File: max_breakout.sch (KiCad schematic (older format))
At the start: 29 parts, among them J1 AVR-JTAG-10, J2 Conn_01x16, J3 Conn_01x16, J4 USB_B_Micro, SW1 SW_DIP_x06, U1 CPLD - EPM7032STC44, X1 KC5032K12.0000C10E00-Oscillat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

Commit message: switched to 32pins
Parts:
- U1: symbol sbc_z80-rescue:EPM7032STC44-CPLD_Altera -> max_breakout-rescue:EPM7032STC44-CPLD_Altera-sbc_z80-rescue
- X1: symbol rc2014_max_v-rescue:KC5032K12.0000C10E00-Oscillator -> max_breakout-rescue:KC5032K12.0000C10E00-Oscillator-rc2014_max_v-rescue
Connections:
- wire segments 174 -> 180
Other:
- moved on the sheet: R15
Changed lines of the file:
@@
 EESchema Schematic File Version 4
-LIBS:sbc_z80-cache
+LIBS:max_breakout-cache
 EELAYER 29 0
 EELAYER END
@@
 $EndDescr
 $Comp
-L sbc_z80-rescue:EPM7032STC44-CPLD_Altera U1
+L max_breakout-rescue:EPM7032STC44-CPLD_Altera-sbc_z80-rescue U1
 U 1 1 5D1470E3
 P 4595 2740
@@
 L Device:C_Small C?
 U 1 1 5D617C96
-P 1005 1585
+P 1046 1798
 AR Path="/5D65A6A0/5D617C96" Ref="C?"  Part="1"
 AR Path="/5D617C96" Ref="C1"  Part="1"
-F 0 "C1" H 1097 1631 50  0000 L CNN
-F 1 "100nF" H 1097 1540 50  0000 L CNN
-F 2 "Capacitor_SMD:C_0603_1608Metric_Pad1.05x0.95mm_HandSolder" H 1005 1585 50  0001 C CNN
-F 3 "https://www.mouser.com/datasheet/2/396/mlcc02_e-1307760.pdf" H 1005 1585 50  0001 C CNN
-F 4 "Multilayer Ceramic Capacitors MLCC - SMD/SMT 0603 6.3V 0.47uF 10% X7R" H 1097 1731 50  0001 C CNN "Description"
-F 5 "Taiyo Yuden" H 1005 1585 50  0001 C CNN "MFR"
-F 6 "JMK107B7474KA-T" H 1005 1585 50  0001 C CNN "MPN"
-F 7 "963-JMK107B7474KA-T" H 1097 1731 50  0001 C CNN "SPN"
-F 8 "Mouser" H 1005 1585 50  0001 C CNN "SPR"
-F 9 "https://www.mouser.com/ProductDetail/963-JMK107B7474KA-T" H 1097 1731 50  0001 C CNN "SPURL"
-	1    1005 1585
+F 0 "C1" H 1138 1844 50  0000 L CNN
+F 1 "100nF" H 1138 1753 50  0000 L CNN
+F 2 "Capacitor_SMD:C_0603_1608Metric_Pad1.05x0.95mm_HandSolder" H 1046 1798 50  0001 C CNN
+F 3 "https://www.mouser.com/datasheet/2/396/mlcc02_e-1307760.pdf" H 1046 1798 50  0001 C CNN
+F 4 "Multilayer Ceramic Capacitors MLCC - SMD/SMT 0603 6.3V 0.47uF 10% X7R" H 1138 1944 50  0001 C CNN "Description"
+F 5 "Taiyo Yuden" H 1046 1798 50  0001 C CNN "MFR"
+F 6 "JMK107B7474KA-T" H 1046 1798 50  0001 C CNN "MPN"
+F 7 "963-JMK107B7474KA-T" H 1138 1944 50  0001 C CNN "SPN"
+F 8 "Mouser" H 1046 1798 50  0001 C CNN "SPR"
+F 9 "https://www.mouser.com/ProductDetail/963-JMK107B7474KA-T" H 1138 1944 50  0001 C CNN "SPURL"
+	1    1046 1798
 	1    0    0    -1
 $EndComp
@@
 $Comp
 L Device:R_Small R?
-U 1 1 5DC500B6
-P 7455 1825
-AR Path="/5D0F9837/5DC500B6" Ref="R?"  Part="1"
-AR Path="/5CFABACD/5D0BF766/5DC500B6" Ref="R?"  Part="1"
-AR Path="/5D1AF052/5DC500B6" Ref="R?"  Part="1"
-AR Path="/5DC500B6" Ref="R3"  Part="1"
-F 0 "R3" H 7320 1860 50  0000 L CNN
-F 1 "10K" H 7315 1785 50  0000 L CNN
-F 2 "Resistor_SMD:R_0603_1608Metric_Pad1.05x0.95mm_HandSolder" H 7455 1825 50  0001 C CNN
-F 3 "~" H 7455 1825 50  0001 C CNN
-	1    7455 1825
-	1    0    0    -1
-$EndComp
-$Comp
-L Device:R_Small R?
 U 1 1 5DCD773D
 P 7565 1825
@@
 	7565 2485 7835 2485
 Wire Wire Line
-	7345 1725 7455 1725
-Connection ~ 7455 1725
-Wire Wire Line
-	7455 1725 7565 1725
-Wire Wire Line
 	3785 5450 3785 5350
 $Comp
@@
 $EndComp
 Wire Wire Line
-	1605 1485 1985 1485
+	1646 1698 2026 1698
 Wire Wire Line
 	3790 5750 3790 5650
@@
 $EndComp
 $Comp
-L rc2014_max_v-rescue:KC5032K12.0000C10E00-Oscillator X1
+L max_breakout-rescue:KC5032K12.0000C10E00-Oscillator-rc2014_max_v-rescue X1
 U 1 1 5D598D88
-P 1305 1485
-F 0 "X1" H 1560 1655 50  0000 L CNN
-F 1 "KC5032K12.0000C10E00-Oscillator" H 1365 1755 50  0000 L CNN
-F 2 "Oscillator:Oscillator_SMD_Fordahl_DFAS15-4Pin_5.0x3.2mm_HandSoldering" H 2005 1135 50  0001 C CNN
-F 3 "" H 1205 1485 50  0001 C CNN
-	1    1305 1485
-	1    0    0    -1
-$EndComp
-Wire Wire Line
-	1005 1485 1005 1185
-Wire Wire Line
-	1005 1185 1305 1185
+P 1346 1698
+F 0 "X1" H 1601 1868 50  0000 L CNN
+F 1 "KC5032K12.0000C10E00-Oscillator" H 1406 1968 50  0000 L CNN
+F 2 "Oscillator:Oscillator_SMD_Fordahl_DFAS15-4Pin_5.0x3.2mm_HandSoldering" H 2046 1348 50  0001 C CNN
+F 3 "" H 1246 1698 50  0001 C CNN
+	1    1346 1698
+	1    0    0    -1
+$EndComp
+Wire Wire Line
+	1046 1698 1046 1398
+Wire Wire Line
+	1046 1398 1346 1398
 $Comp
 L power:+5V #PWR01
 U 1 1 5D5A86C9
-P 1305 1185
-F 0 "#PWR01" H 1305 1035 50  0001 C CNN
-F 1 "+5V" H 1320 1358 50  0000 C CNN
-F 2 "" H 1305 1185 50  0001 C CNN
-F 3 "" H 1305 1185 50  0001 C CNN
-	1    1305 1185
-	1    0    0    -1
-$EndComp
-Connection ~ 1005 1485
-Wire Wire Line
-	1005 1685 1005 1830
-Wire Wire Line
-	1005 1830 1305 1830
-Wire Wire Line
-	1305 1830 1305 1785
-Text Label 1645 1485 0    50   ~ 0
+P 1346 1398
+F 0 "#PWR01" H 1346 1248 50  0001 C CNN
+F 1 "+5V" H 1361 1571 50  0000 C CNN
+F 2 "" H 1346 1398 50  0001 C CNN
+F 3 "" H 1346 1398 50  0001 C CNN
+	1    1346 1398
+	1    0    0    -1
+$EndComp
+Connection ~ 1046 1698
+Wire Wire Line
+	1046 1898 1046 2043
+Wire Wire Line
+	1046 2043 1346 2043
+Wire Wire Line
+	1346 2043 1346 1998
+Text Label 1686 1698 0    50   ~ 0
 CLK1
 $Comp
@@
 Wire Wire Line
 	10085 2745 9825 2745
-Wire Bus Line
-	8315 3115 8315 3365
 $Comp
 L Device:LED D1
 U 1 1 5D74CDCC
-P 2760 4405
-F 0 "D1" H 2753 4621 50  0000 C CNN
-F 1 "LED" H 2753 4530 50  0000 C CNN
-F 2 "LED_SMD:LED_0603_1608Metric_Pad1.05x0.95mm_HandSolder" H 2760 4405 50  0001 C CNN
-F 3 "~" H 2760 4405 50  0001 C CNN
-	1    2760 4405
+P 1498 4856
+F 0 "D1" H 1491 5072 50  0000 C CNN
+F 1 "LED" H 1491 4981 50  0000 C CNN
+F 2 "LED_SMD:LED_0603_1608Metric_Pad1.05x0.95mm_HandSolder" H 1498 4856 50  0001 C CNN
+F 3 "~" H 1498 4856 50  0001 C CNN
+	1    1498 4856
 	1    0    0    -1
 $EndComp
@@
 L power:GND #PWR018
 U 1 1 5D74F3FF
-P 2315 4685
+P 1053 5136
 AR Path="/5D74F3FF" Ref="#PWR018"  Part="1"
 AR Path="/5CB63856/5D74F3FF" Ref="#PWR?"  Part="1"
@@
 AR Path="/5CFABACD/5D0BF766/5D74F3FF" Ref="#PWR?"  Part="1"
 AR Path="/5D1AF052/5D74F3FF" Ref="#PWR?"  Part="1"
-F 0 "#PWR018" H 2315 4435 50  0001 C CNN
-F 1 "GND" H 2320 4512 50  0000 C CNN
-F 2 "" H 2315 4685 50  0001 C CNN
-F 3 "" H 2315 4685 50  0001 C CNN
-	1    2315 4685
+F 0 "#PWR018" H 1053 4886 50  0001 C CNN
+F 1 "GND" H 1058 4963 50  0000 C CNN
+F 2 "" H 1053 5136 50  0001 C CNN
+F 3 "" H 1053 5136 50  0001 C CNN
+	1    1053 5136
 	0    -1   -1   0
 $EndComp
 Wire Wire Line
-	2255 4405 2255 4685
-Wire Wire Line
-	2255 4685 2315 4685
+	993  4856 993  5136
+Wire Wire Line
+	993  5136 1053 5136
 $Comp
 L Device:R_Small R?
 U 1 1 5D74F407
-P 2510 4405
+P 1248 4856
 AR Path="/5D0F9837/5D74F407" Ref="R?"  Part="1"
 AR Path="/5CFABACD/5D0BF766/5D74F407" Ref="R?"  Part="1"
 AR Path="/5D1AF052/5D74F407" Ref="R?"  Part="1"
 AR Path="/5D74F407" Ref="R15"  Part="1"
-F 0 "R15" H 2375 4440 50  0000 L CNN
-F 1 "1K" H 2370 4365 50  0000 L CNN
-F 2 "Resistor_SMD:R_0603_1608Metric_Pad1.05x0.95mm_HandSolder" H 2510 4405 50  0001 C CNN
-F 3 "~" H 2510 4405 50  0001 C CNN
-	1    2510 4405
+F 0 "R15" H 1113 4891 50  0000 L CNN
+F 1 "1K" H 1108 4816 50  0000 L CNN
+F 2 "Resistor_SMD:R_0603_1608Metric_Pad1.05x0.95mm_HandSolder" H 1248 4856 50  0001 C CNN
+F 3 "~" H 1248 4856 50  0001 C CNN
+	1    1248 4856
 	0    -1   -1   0
 $EndComp
 Wire Wire Line
-	2255 4405 2410 4405
-Wire Wire Line
-	2910 4405 3150 4405
+	993  4856 1148 4856
+Wire Wire Line
+	1648 4856 1888 4856
 $Comp
 L power:+5V #PWR017
 U 1 1 5D77C61D
-P 3150 4405
-F 0 "#PWR017" H 3150 4255 50  0001 C CNN
-F 1 "+5V" H 3165 4578 50  0000 C CNN
-F 2 "" H 3150 4405 50  0001 C CNN
-F 3 "" H 3150 4405 50  0001 C CNN
-	1    3150 4405
+P 1888 4856
+F 0 "#PWR017" H 1888 4706 50  0001 C CNN
+F 1 "+5V" H 1903 5029 50  0000 C CNN
+F 2 "" H 1888 4856 50  0001 C CNN
+F 3 "" H 1888 4856 50  0001 C CNN
+	1    1888 4856
 	1    0    0    -1
 $EndComp
@@
 L power:GND #PWR0101
 U 1 1 5D838E8D
-P 1305 1830
+P 1346 2043
 AR Path="/5D838E8D" Ref="#PWR0101"  Part="1"
 AR Path="/5CB63856/5D838E8D" Ref="#PWR?"  Part="1"
@@
 AR Path="/5CFABACD/5D838E8D" Ref="#PWR?"  Part="1"
 AR Path="/5CF9C1ED/5D838E8D" Ref="#PWR?"  Part="1"
-F 0 "#PWR0101" H 1305 1580 50  0001 C CNN
-F 1 "GND" H 1310 1657 50  0000 C CNN
-F 2 "" H 1305 1830 50  0001 C CNN
-F 3 "" H 1305 1830 50  0001 C CNN
-	1    1305 1830
-	1    0    0    -1
-$EndComp
-Connection ~ 1305 1830
+F 0 "#PWR0101" H 1346 1793 50  0001 C CNN
+F 1 "GND" H 1351 1870 50  0000 C CNN
+F 2 "" H 1346 2043 50  0001 C CNN
+F 3 "" H 1346 2043 50  0001 C CNN
+	1    1346 2043
+	1    0    0    -1
+$EndComp
+Connection ~ 1346 2043
 Wire Wire Line
 	1600 2930 2155 2930
@@
 	1    0    0    -1
 $EndComp
-$Comp
-L power:+5V #PWR0102
-U 1 1 5DA0BC85
-P 7455 1570
-F 0 "#PWR0102" H 7455 1420 50  0001 C CNN
-F 1 "+5V" H 7470 1743 50  0000 C CNN
-F 2 "" H 7455 1570 50  0001 C CNN
-F 3 "" H 7455 1570 50  0001 C CNN
-	1    7455 1570
-	1    0    0    -1
-$EndComp
-Wire Wire Line
-	7455 1570 7455 1725
 Entry Wire Line
 	9725 1745 9825 1845
@@
 Text Label 9885 2145 0    50   ~ 0
 B19
+Wire Bus Line
+	8313 2905 8316 2905
+Connection ~ 1346 1398
+$Comp
+L Device:R_Small R?
+U 1 1 5DC500B6
+P 7455 1825
+AR Path="/5D0F9837/5DC500B6" Ref="R?"  Part="1"
+AR Path="/5CFABACD/5D0BF766/5DC500B6" Ref="R?"  Part="1"
+AR Path="/5D1AF052/5DC500B6" Ref="R?"  Part="1"
+AR Path="/5DC500B6" Ref="R3"  Part="1"
+F 0 "R3" H 7320 1860 50  0000 L CNN
+F 1 "10K" H 7315 1785 50  0000 L CNN
+F 2 "Resistor_SMD:R_0603_1608Metric_Pad1.05x0.95mm_HandSolder" H 7455 1825 50  0001 C CNN
+F 3 "~" H 7455 1825 50  0001 C CNN
+	1    7455 1825
+	1    0    0    -1
+$EndComp
+Wire Wire Line
+	7345 1728 7345 1725
+Wire Wire Line
+	7345 1588 7565 1588
+Wire Wire Line
+	7565 1588 7565 1725
+Connection ~ 7345 1725
+Wire Wire Line
+	7345 1725 7345 1588
+Connection ~ 7565 1725
+Wire Wire Line
+	7565 1725 7565 1728
+Wire Wire Line
+	7455 1726 7455 1725
+Connection ~ 7455 1725
+$Comp
+L power:+5V #PWR0102
+U 1 1 5D46CB3B
+P 7455 1527
+F 0 "#PWR0102" H 7455 1377 50  0001 C CNN
+F 1 "+5V" H 7470 1700 50  0000 C CNN
+F 2 "" H 7455 1527 50  0001 C CNN
+F 3 "" H 7455 1527 50  0001 C CNN
+	1    7455 1527
+	1    0    0    -1
+$EndComp
+Wire Wire Line
+	7455 1526 7456 1526
+Wire Wire Line
+	7455 1526 7455 1527
+Connection ~ 7455 1527
+Wire Wire Line
+	7455 1527 7455 1725
 Wire Bus Line
 	3685 3300 3685 3605
@@
 	5505 1455 5505 3150
 Wire Bus Line
-	8315 1310 8315 3110
+	8315 1317 8315 2904
 Wire Bus Line
-	9725 1360 9725 3370
+	9725 1384 9725 2984
 Wire Bus Line
 	3685 1495 3685 3295

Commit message: reorganized parts
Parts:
- J1: footprint Connector_Multicomp:Multicomp_MC9A12-1034_2x05_P2.54mm_Vertical -> Connector_PinHeader_2.54mm:PinHeader_2x05_P2.54mm_Vertical
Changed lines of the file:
@@
 F 0 "J1" H 6485 2285 50  0000 R CNN
 F 1 "AVR-JTAG-10" H 6205 2785 50  0000 R CNN
-F 2 "Connector_Multicomp:Multicomp_MC9A12-1034_2x05_P2.54mm_Vertical" V 6295 2435 50  0001 C CNN
+F 2 "Connector_PinHeader_2.54mm:PinHeader_2x05_P2.54mm_Vertical" V 6295 2435 50  0001 C CNN
 F 3 "~" H 5170 1735 50  0001 C CNN
 	1    6445 2285

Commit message: removed bus
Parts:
- removed R2, R3, R4: 10K, Resistor_SMD:R_0603_1608Metric_Pad1.05x0.95mm_HandSolder, symbol Device:R_Small
- added R2, R3, R4: 10K, Resistor_SMD:R_0603_1608Metric_Pad1.05x0.95mm_HandSolder, symbol max_breakout-rescue:R_Small-Device
- C1, C3, C4, C5, C6: symbol Device:C_Small -> max_breakout-rescue:C_Small-Device
- C2: symbol Device:C -> max_breakout-rescue:C-Device
- D1: symbol Device:LED -> max_breakout-rescue:LED-Device
- J1: symbol Connector:AVR-JTAG-10 -> max_breakout-rescue:AVR-JTAG-10-Connector
- J2, J3: symbol Connector_Generic:Conn_01x16 -> max_breakout-rescue:Conn_01x16-Connector_Generic
- J4: symbol Connector:USB_B_Micro -> max_breakout-rescue:USB_B_Micro-Connector
- R1, R10, R11, R12, R13, R14, R15, R6, R7, R8, R9: symbol Device:R_Small -> max_breakout-rescue:R_Small-Device
- R5: symbol Device:R -> max_breakout-rescue:R-Device
- SW1: symbol Switch:SW_DIP_x06 -> max_breakout-rescue:SW_DIP_x06-Switch
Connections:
- wire segments 180 -> 171
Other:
- moved on the sheet: R1

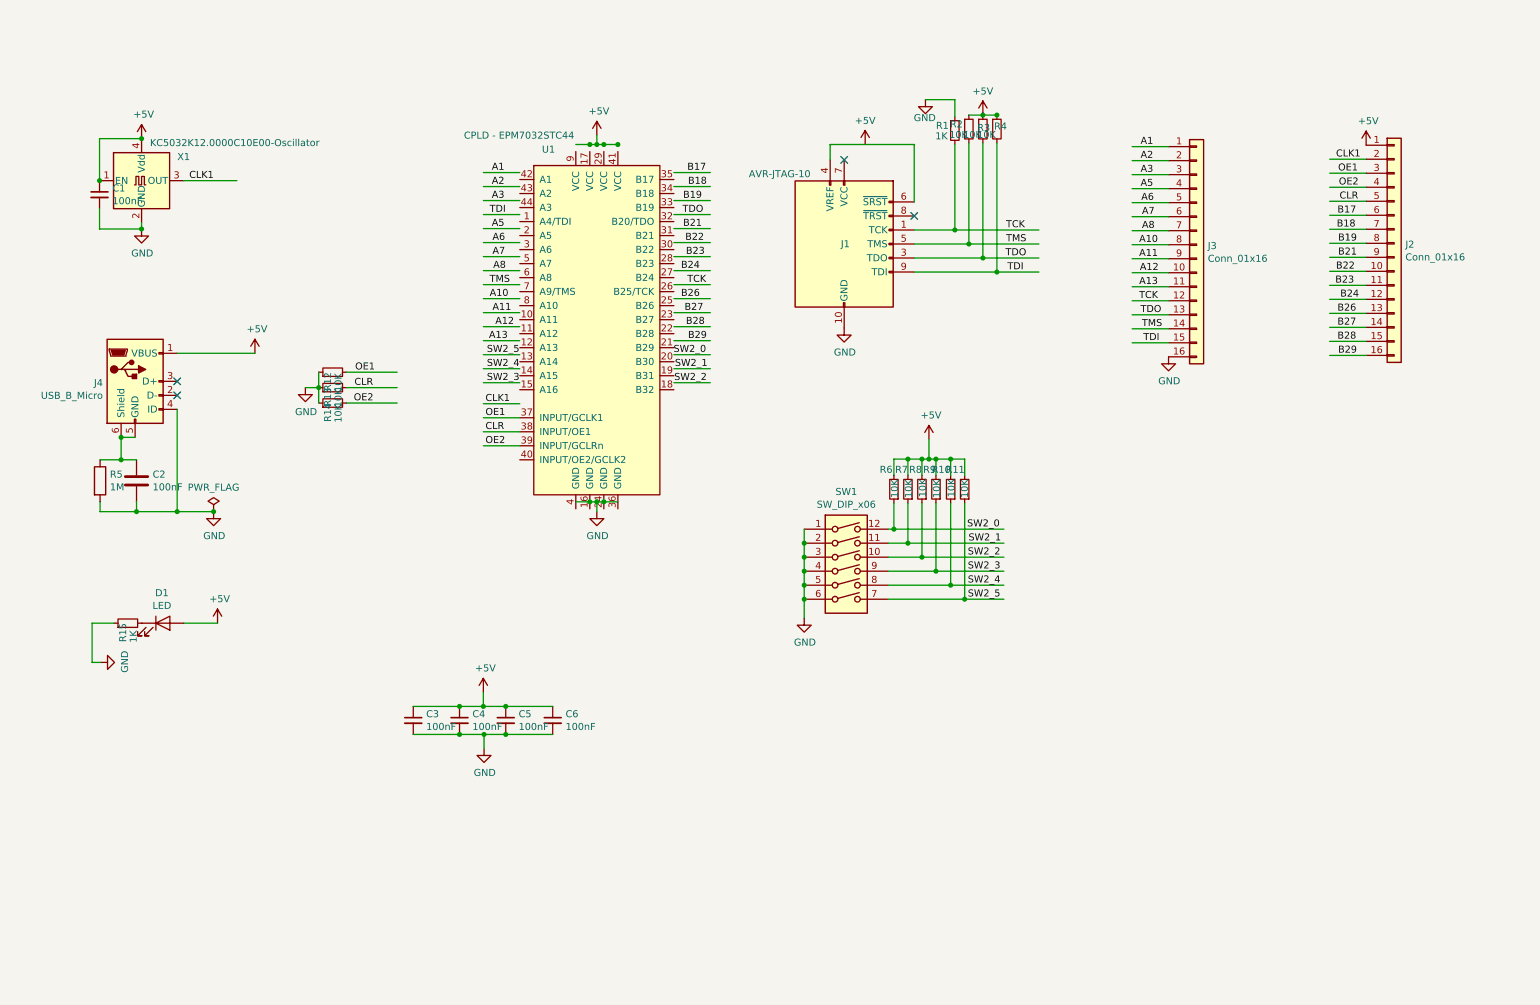
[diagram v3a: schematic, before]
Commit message: added voltage stepdown for xtal
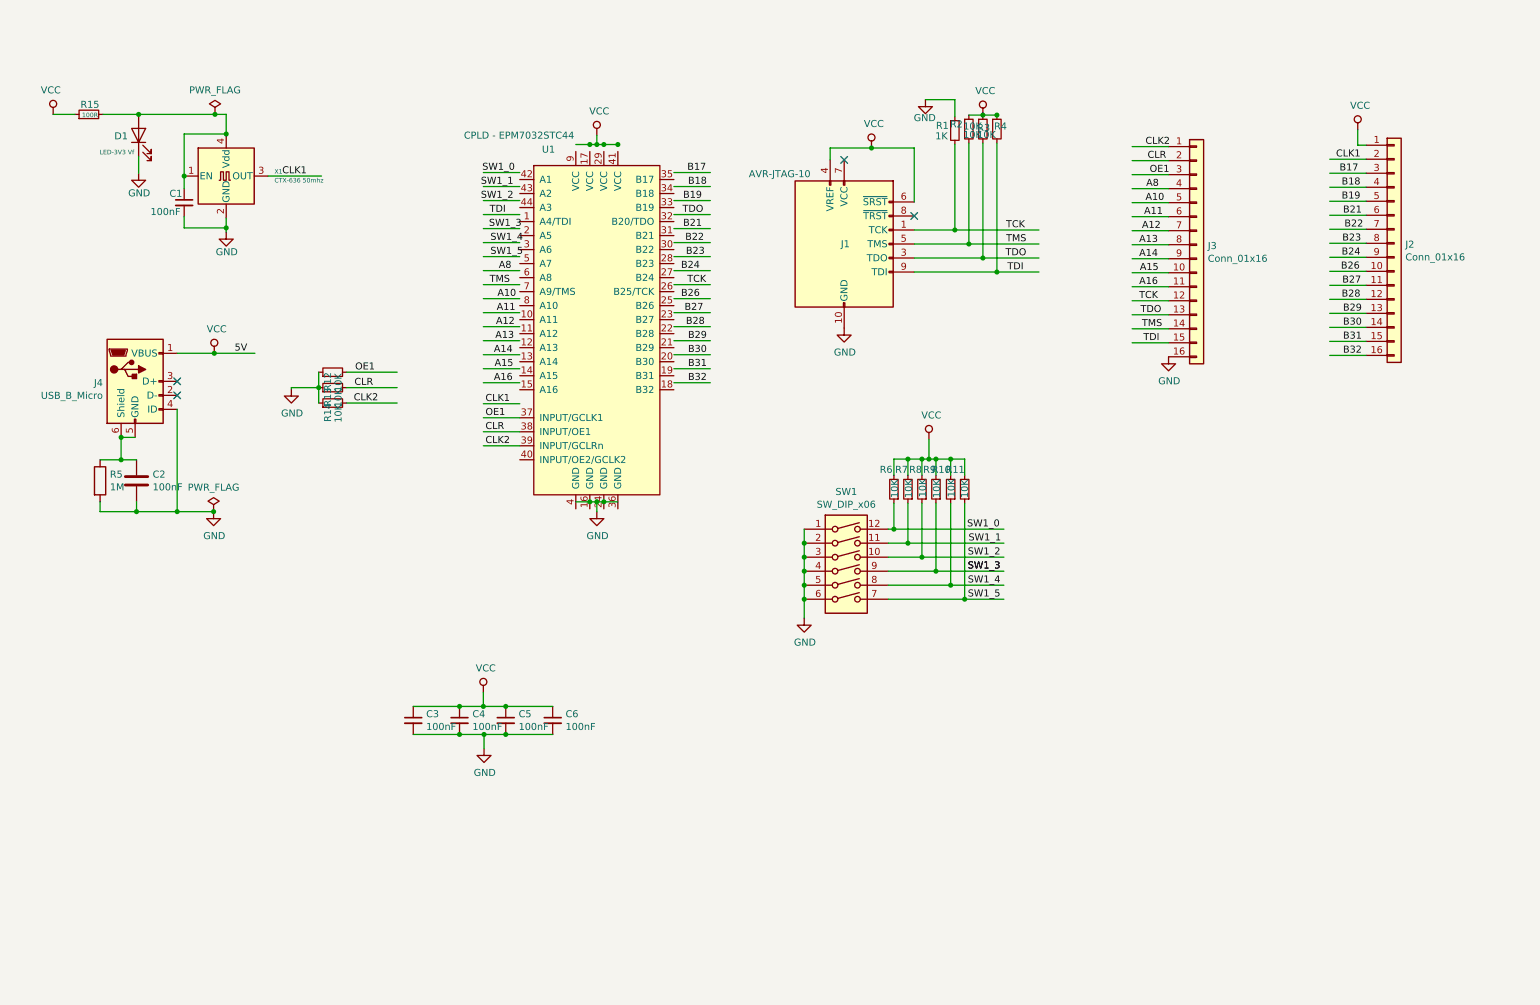
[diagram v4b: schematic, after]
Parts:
- removed X1: KC5032K12.0000C10E00-Oscillator, Oscillator:Oscillator_SMD_Fordahl_DFAS15-4Pin_5.0x3.2mm_HandSoldering, symbol max_breakout-rescue:KC5032K12.0000C10E00-Oscillator-rc2014_max_v-rescue
- added X1: CTX-636 50mhz, Oscillator:Oscillator_SMD_TXC_7C-4Pin_5.0x3.2mm_HandSoldering, symbol Oscillator:TXC-7C
- D1: value LED -> LED-3V3 Vf
- R15: value 1K -> 100R
- SW1: footprint Button_Switch_SMD:SW_DIP_SPSTx06_Slide_Copal_CHS-06A_W5.08mm_P1.27mm_JPin -> Button_Switch_SMD:SW_DIP_SPSTx06_Slide_Omron_A6H-6101_W6.15mm_P1.27mm
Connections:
- net labels added: 5V, A14, A15, A16, B30, B31, B32, CLK2, SW1_0, SW1_1, SW1_2, SW1_3, SW1_4, SW1_5, VCC
- net labels removed: +5V, A1, A2, A3, A5, A6, A7, OE2, SW2_0, SW2_1, SW2_2, SW2_3, SW2_4, SW2_5
- wire segments 171 -> 181
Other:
- moved on the sheet: D1, R15

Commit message: finished layout
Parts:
- added C2: 10uF, Capacitor_SMD:C_0603_1608Metric_Pad1.05x0.95mm_HandSolder, symbol max_breakout-rescue:C_Small-Device
- added C3: 100nF, Capacitor_SMD:C_0603_1608Metric_Pad1.05x0.95mm_HandSolder, symbol max_breakout-rescue:C_Small-Device
- added D2: LED-3V3 Vf, LED_SMD:LED_0603_1608Metric_Pad1.05x0.95mm_HandSolder, symbol max_breakout-rescue:LED-Device
- added D3: LED, LED_SMD:LED_2C_0603_1608Metric_Pad1.05x0.95mm_HandSolder, symbol Device:LED_Dual_ACAC
- added D4: D_Schottky_Small, Diode_SMD:D_SOD-323_HandSoldering, symbol Device:D_Schottky_Small
- added JP1: LED_EN, Connector_PinHeader_1.27mm:PinHeader_1x02_P1.27mm_Vertical, symbol Jumper:Jumper_2_Open
- added JP2: SW_EN, Connector_PinHeader_1.27mm:PinHeader_1x02_P1.27mm_Vertical, symbol Jumper:Jumper_2_Open
- added Q1: IRLML6402, Package_TO_SOT_SMD:SOT-23, symbol Transistor_FET:IRLML6402
- added R11: 360R, Resistor_SMD:R_0603_1608Metric_Pad1.05x0.95mm_HandSolder, symbol max_breakout-rescue:R_Small-Device
- added R13, R22: 10K, Resistor_SMD:R_0603_1608Metric_Pad1.05x0.95mm_HandSolder, symbol max_breakout-rescue:R_Small-Device
- added R20, R21: 360R, Resistor_SMD:R_0603_1608Metric_Pad1.05x0.95mm_HandSolder, symbol Device:R_Small
- added R6, R8: 100R, Resistor_SMD:R_0603_1608Metric_Pad1.05x0.95mm_HandSolder, symbol max_breakout-rescue:R_Small-Device
- added U2: 74HCT2G125, Package_SO:TSSOP-8_3x3mm_P0.65mm, symbol 74xGxx:74HCT2G125
- added U3: 74HCT365, Package_SO:TSSOP-16_4.4x5mm_P0.65mm, symbol 74xx:74HCT365
- J3: renamed from J2; value Conn_01x16 -> Conn_01x19; footprint Connector_PinHeader_2.54mm:PinHeader_1x16_P2.54mm_Vertical -> Connector_PinHeader_2.54mm:PinHeader_1x19_P2.54mm_Vertical; symbol max_breakout-rescue:Conn_01x16-Connector_Generic -> Connector_Generic:Conn_01x19
- J4: renamed from J3; value Conn_01x16 -> Conn_01x19; footprint Connector_PinHeader_2.54mm:PinHeader_1x16_P2.54mm_Vertical -> Connector_PinHeader_2.54mm:PinHeader_1x19_P2.54mm_Vertical; symbol max_breakout-rescue:Conn_01x16-Connector_Generic -> Connector_Generic:Conn_01x19
- renumbered C2 to C4, C3 to C5, C4 to C6, C5 to C7, C6 to C8, J4 to J2, R15 to R1, R14 to R10, R5 to R12, R6 to R14, R7 to R15, R8 to R16, R9 to R17, R10 to R18, R11 to R19, R1 to R5, R12 to R7, R13 to R9
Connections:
- net labels added: 5V_in, A1, A2, A3, A5, A6, A7, LED_ENA, SW_ENA
- net labels removed: SW1_0, SW1_1, SW1_2, SW1_3, SW1_4, SW1_5
- wire segments 181 -> 218
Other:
- note added: "USER GPIO"
- moved on the sheet: C1, C4, C5, C6, C7, C8, D1, J1, J2, R1, R10, R12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

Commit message: checkpoint
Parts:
- removed C3: 100nF, Capacitor_SMD:C_0603_1608Metric_Pad1.05x0.95mm_HandSolder, symbol max_breakout-rescue:C_Small-Device
- removed D4: D_Schottky_Small, Diode_SMD:D_SOD-323_HandSoldering, symbol Device:D_Schottky_Small
- added C10, C8, C9: .33uF, Capacitor_SMD:C_0603_1608Metric_Pad1.05x0.95mm_HandSolder, symbol max_breakout-rescue:C_Small-Device
- added U4, U5: MAX40200AUK, Package_TO_SOT_SMD:SOT-23-5_HandSoldering, symbol Analog_Switch:MAX40200AUK
- added U6, U7: 74AHCT1G04, Package_TO_SOT_SMD:SOT-23-5_HandSoldering, symbol 74xGxx:74AHCT1G04
- C7: renamed from C2; value 10uF -> .33uF
- U1: renamed from U3; symbol 74xx:74HCT365 -> max_breakout-rescue:74HCT365-74xx
- U3: renamed from U2; symbol 74xGxx:74HCT2G125 -> max_breakout-rescue:74HCT2G125-74xGxx
- renumbered C5 to C2, C6 to C3, C7 to C4, C8 to C5, C4 to C6, D3 to D2, D2 to D3, J4 to J2, J2 to J3, J3 to J4, JP2 to JP1, JP1 to JP2, R22 to R1, R7 to R10, R9 to R11, R10 to R12, R20 to R13, R21 to R14, R13 to R15, R5 to R16, R8 to R17, R2 to R18, R3 to R19, R1 to R2, R4 to R20, R11 to R21, R12 to R22, R14 to R3, R15 to R4, R16 to R5, R17 to R6, R18 to R7, R19 to R8, R6 to R9, U1 to U2
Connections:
- net labels added: 5V_USB
- net labels removed: 5V
- wire segments 218 -> 234
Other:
- note added: "50Mhz Clock"
- note added: "JTAG"
- moved on the sheet: C1, C2, C3, C4, C5, C6, C7, D1, D2, D3, J2, J3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

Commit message: start routing
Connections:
- wire segments 234 -> 226
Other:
- moved on the sheet: C10, C2, C3, C4, C5, C6, C7, C8, D3, J1, J3, JP1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
